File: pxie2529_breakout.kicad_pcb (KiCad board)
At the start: 2 copper layers, 1 part, among them J1 connector-25x4

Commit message: finished routing
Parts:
- added J2: Conn_02x25_Odd_Even, Connector_IDC:IDC-Header_2x25_P2.54mm_Latch12.0mm_Vertical, F.Cu at (102.0, 78.5)
- added J3: Conn_02x25_Odd_Even, Connector_IDC:IDC-Header_2x25_P2.54mm_Latch12.0mm_Vertical, F.Cu at (113.9, 78.5)
- moved J1 20.4 mm to (67.0, 109.0)
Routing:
- net /B0R2+: track 0.00 -> 48.8 mm
- net /B1C0+: track 0.00 -> 48.7 mm
- net /B0C2+: track 0.00 -> 48.7 mm
- net /B1C2+: track 0.00 -> 48.7 mm
- net /B1R0+: track 0.00 -> 48.7 mm
- net /B1C9+: track 0.00 -> 48.7 mm
- net /B1C11+: track 0.00 -> 48.7 mm
- net /B0R0+: track 0.00 -> 48.7 mm
- net /B0C0+: track 0.00 -> 48.7 mm
- net /B0C10+: track 0.00 -> 48.7 mm
- net /B1C1+: track 0.00 -> 48.7 mm
- net /B1R2+: track 0.00 -> 48.7 mm
- net /B0C8+: track 0.00 -> 48.7 mm
- net /B1C8+: track 0.00 -> 48.7 mm
- net /B1C3+: track 0.00 -> 48.7 mm
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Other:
- board outline added: 69.2 x 103 mm
- net class Default: clearance 0.2 -> 0.125; trace_width 0.25 -> 0.2; via_dia 0.8 -> 0.6; via_drill 0.4 -> 0.3
- rule trace_clearance: 0.2 -> 0.125
- rule trace_min: 0.2 -> 0.125
- rule via_min_size: 0.4 -> 0.6

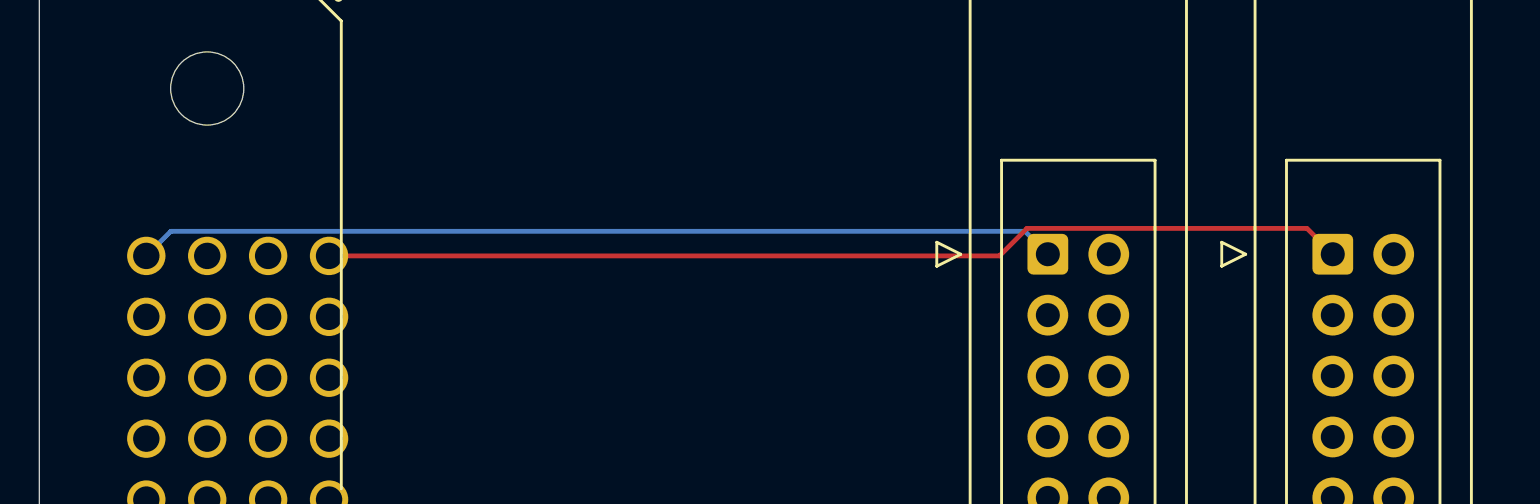
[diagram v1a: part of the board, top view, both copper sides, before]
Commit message: ground connection added
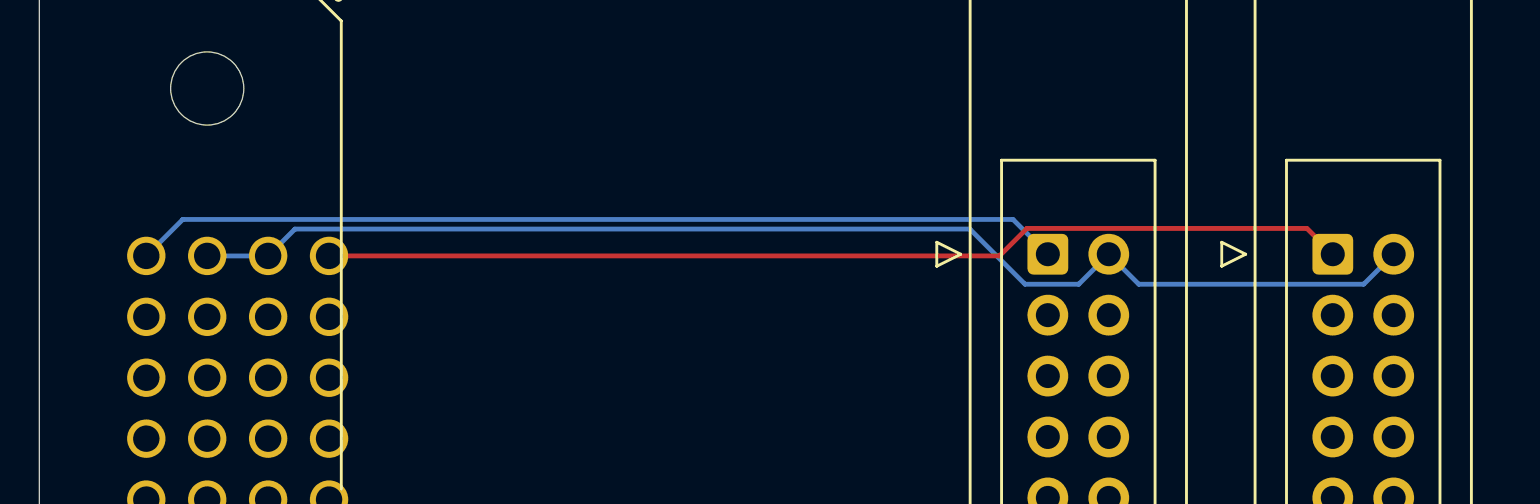
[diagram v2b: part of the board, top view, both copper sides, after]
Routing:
- net /GND: track 0.00 -> 52.4 mm

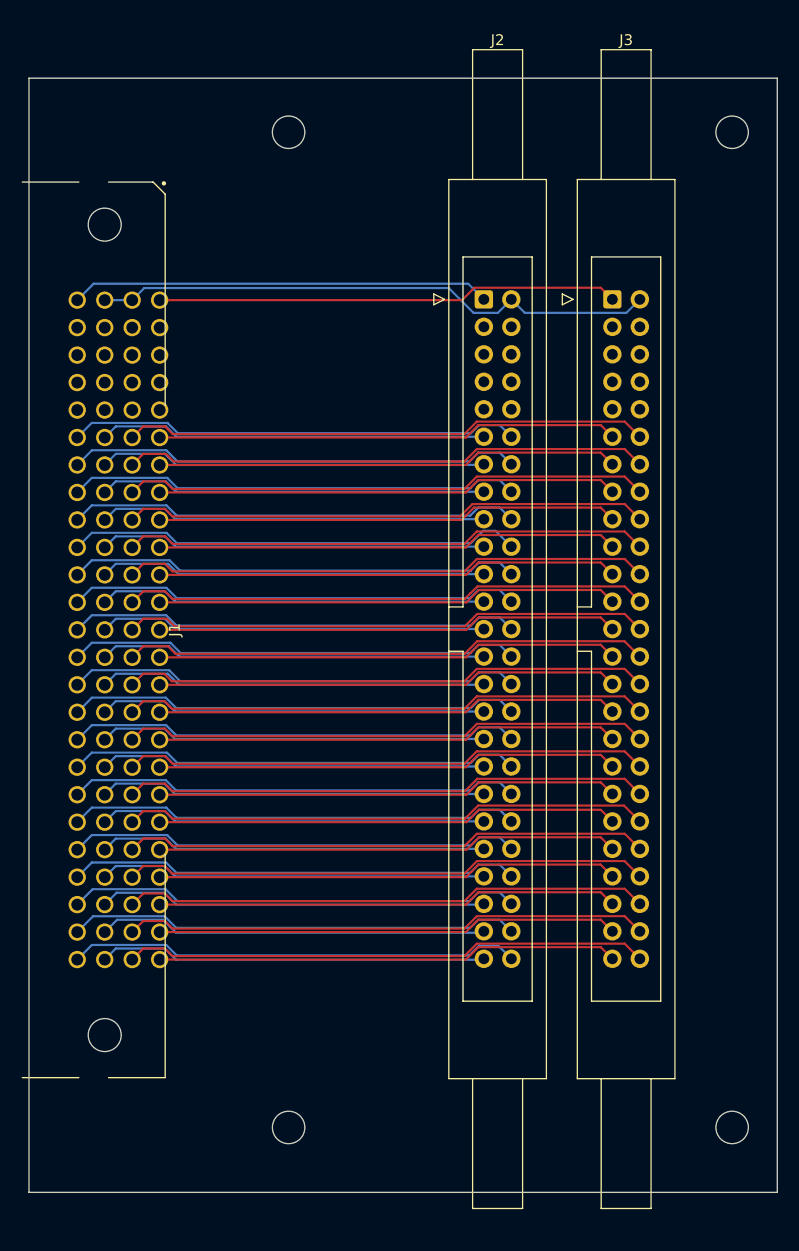
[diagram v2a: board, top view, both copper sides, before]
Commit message: fixed connector orientation
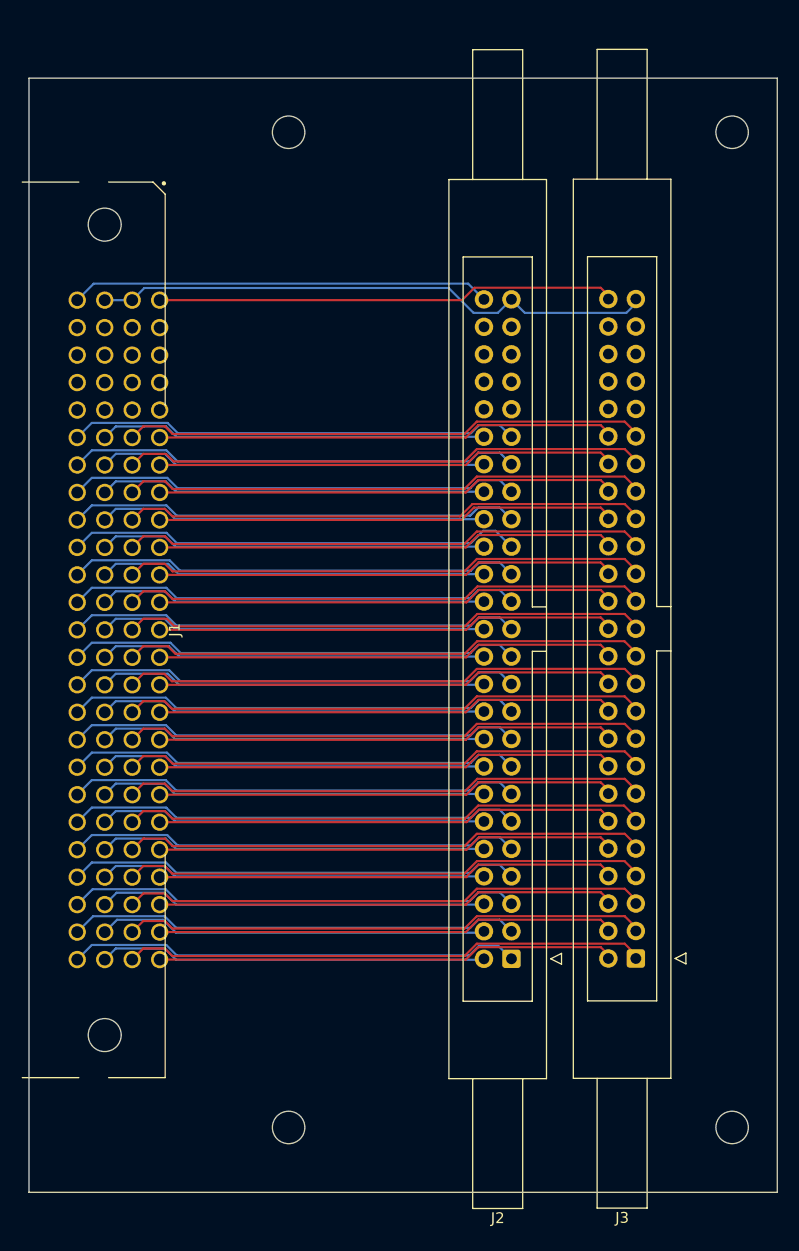
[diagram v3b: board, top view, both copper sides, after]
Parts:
- moved J2 61.0 mm to (104.6, 139.4), turned to 180 degrees
- moved J3 61.0 mm to (116.1, 139.4), turned to 180 degrees
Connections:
- J2 pad 1: /TRIGIN -> /B0R1-
- J2 pad 10: Net-(J2-Pad10) -> /B0C7+
- J2 pad 11: /B1C15+ -> /B0R3-
- J2 pad 12: /B1C15- -> /B0R3+
- J2 pad 13: /B1C14+ -> /B0C12-
- J2 pad 14: /B1C14- -> /B0C12+
- J2 pad 15: /B1C13+ -> /B0C13-
- J2 pad 16: /B1C13- -> /B0C13+
- J2 pad 17: /B1C12+ -> /B0C14-
- J2 pad 18: /B1C12- -> /B0C14+
- J2 pad 19: /B1R3+ -> /B0C15-
- J2 pad 2: /GND -> /B0R1+
- J2 pad 20: /B1R3- -> /B0C15+
- J2 pad 21: /B1C7+ -> /B1R1-
- J2 pad 22: /B1C7- -> /B1R1+
- J2 pad 23: /B1C6+ -> /B1C4-
- J2 pad 24: /B1C6- -> /B1C4+
- J2 pad 25: /B1C5+ -> /B1C5-
- J2 pad 26: /B1C5- -> /B1C5+
- J2 pad 27: /B1C4+ -> /B1C6-
- J2 pad 28: /B1C4- -> /B1C6+
- J2 pad 29: /B1R1+ -> /B1C7-
- J2 pad 3: Net-(J2-Pad3) -> /B0C4-
- J2 pad 30: /B1R1- -> /B1C7+
- J2 pad 31: /B0C15+ -> /B1R3-
- J2 pad 32: /B0C15- -> /B1R3+
- J2 pad 33: /B0C14+ -> /B1C12-
- J2 pad 34: /B0C14- -> /B1C12+
- J2 pad 35: /B0C13+ -> /B1C13-
- J2 pad 36: /B0C13- -> /B1C13+
- J2 pad 37: /B0C12+ -> /B1C14-
- J2 pad 38: /B0C12- -> /B1C14+
- J2 pad 39: /B0R3+ -> /B1C15-
- J2 pad 4: Net-(J2-Pad4) -> /B0C4+
- J2 pad 40: /B0R3- -> /B1C15+
- J2 pad 41: /B0C7+ -> Net-(J2-Pad41)
- J2 pad 42: /B0C7- -> Net-(J2-Pad42)
- J2 pad 43: /B0C6+ -> Net-(J2-Pad43)
- J2 pad 44: /B0C6- -> Net-(J2-Pad44)
- J2 pad 45: /B0C5+ -> Net-(J2-Pad45)
- J2 pad 46: /B0C5- -> Net-(J2-Pad46)
- J2 pad 47: /B0C4+ -> Net-(J2-Pad47)
- J2 pad 48: /B0C4- -> Net-(J2-Pad48)
- J2 pad 49: /B0R1+ -> /GND
- J2 pad 5: Net-(J2-Pad5) -> /B0C5-
- J2 pad 50: /B0R1- -> /TRIGIN
- J2 pad 6: Net-(J2-Pad6) -> /B0C5+
- J2 pad 7: Net-(J2-Pad7) -> /B0C6-
- J2 pad 8: Net-(J2-Pad8) -> /B0C6+
- J2 pad 9: Net-(J2-Pad9) -> /B0C7-
- J3 pad 1: /TRIGOUT -> /B0R0+
- J3 pad 10: Net-(J3-Pad10) -> /B0C3-
- J3 pad 11: /B1C11- -> /B0R2+
- J3 pad 12: /B1C11+ -> /B0R2-
- J3 pad 13: /B1C10- -> /B0C8+
- J3 pad 14: /B1C10+ -> /B0C8-
- J3 pad 15: /B1C9- -> /B0C9+
- J3 pad 16: /B1C9+ -> /B0C9-
- J3 pad 17: /B1C8- -> /B0C10+
- J3 pad 18: /B1C8+ -> /B0C10-
- J3 pad 19: /B1R2- -> /B0C11+
- J3 pad 2: /GND -> /B0R0-
- J3 pad 20: /B1R2+ -> /B0C11-
- J3 pad 21: /B1C3- -> /B1R0+
- J3 pad 22: /B1C3+ -> /B1R0-
- J3 pad 23: /B1C2- -> /B1C0+
- J3 pad 24: /B1C2+ -> /B1C0-
- J3 pad 25: /B1C1- -> /B1C1+
- J3 pad 26: /B1C1+ -> /B1C1-
- J3 pad 27: /B1C0- -> /B1C2+
- J3 pad 28: /B1C0+ -> /B1C2-
- J3 pad 29: /B1R0- -> /B1C3+
- J3 pad 3: Net-(J3-Pad3) -> /B0C0+
- J3 pad 30: /B1R0+ -> /B1C3-
- J3 pad 31: /B0C11- -> /B1R2+
- J3 pad 32: /B0C11+ -> /B1R2-
- J3 pad 33: /B0C10- -> /B1C8+
- J3 pad 34: /B0C10+ -> /B1C8-
- J3 pad 35: /B0C9- -> /B1C9+
- J3 pad 36: /B0C9+ -> /B1C9-
- J3 pad 37: /B0C8- -> /B1C10+
- J3 pad 38: /B0C8+ -> /B1C10-
- J3 pad 39: /B0R2- -> /B1C11+
- J3 pad 4: Net-(J3-Pad4) -> /B0C0-
- J3 pad 40: /B0R2+ -> /B1C11-
- J3 pad 41: /B0C3- -> Net-(J3-Pad41)
- J3 pad 42: /B0C3+ -> Net-(J3-Pad42)
- J3 pad 43: /B0C2- -> Net-(J3-Pad43)
- J3 pad 44: /B0C2+ -> Net-(J3-Pad44)
- J3 pad 45: /B0C1- -> Net-(J3-Pad45)
- J3 pad 46: /B0C1+ -> Net-(J3-Pad46)
- J3 pad 47: /B0C0- -> Net-(J3-Pad47)
- J3 pad 48: /B0C0+ -> Net-(J3-Pad48)
- J3 pad 49: /B0R0- -> /GND
- J3 pad 5: Net-(J3-Pad5) -> /B0C1+
- J3 pad 50: /B0R0+ -> /TRIGOUT
- J3 pad 6: Net-(J3-Pad6) -> /B0C1-
- J3 pad 7: Net-(J3-Pad7) -> /B0C2+
- J3 pad 8: Net-(J3-Pad8) -> /B0C2-
- J3 pad 9: Net-(J3-Pad9) -> /B0C3+
